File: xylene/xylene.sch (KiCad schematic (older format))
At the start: 19 parts, among them J1 Conn2, J2 Conn1, U1 DIP-8, U2 LMC555, U3 DIP-16

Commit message: Change 555 to SO-8
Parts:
- U2: footprint Package_SO:VSSOP-8_3.0x3.0mm_P0.65mm -> Package_SO:SO-8_3.9x4.9mm_P1.27mm
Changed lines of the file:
@@
 F 0 "U2" H 5550 5600 50  0000 C CNN
 F 1 "LMC555" H 6050 5600 50  0000 C CNN
-F 2 "Package_SO:VSSOP-8_3.0x3.0mm_P0.65mm" H 6700 4850 50  0001 C CNN
+F 2 "Package_SO:SO-8_3.9x4.9mm_P1.27mm" H 6700 4850 50  0001 C CNN
 F 3 "http://www.ti.com/lit/ds/symlink/lmc555.pdf" H 6700 4850 50  0001 C CNN
 	1    5850 5250

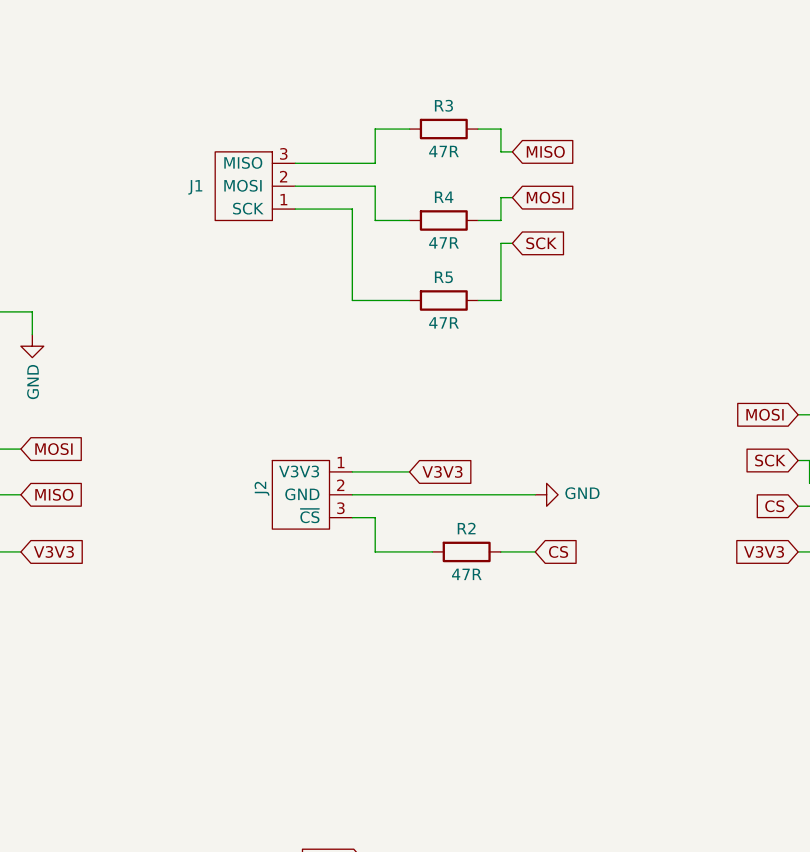
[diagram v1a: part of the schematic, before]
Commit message: Add second pins for logic analyzer
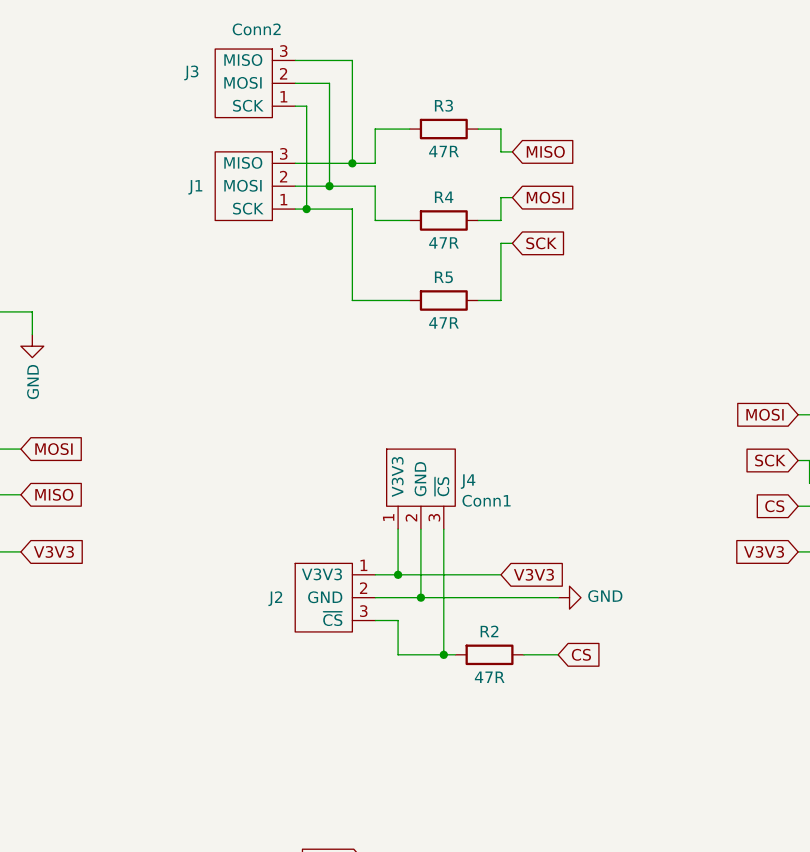
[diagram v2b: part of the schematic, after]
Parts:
- added J3: Conn2, Connector_PinHeader_2.54mm:PinHeader_1x03_P2.54mm_Vertical, symbol xylene:Conn2
- added J4: Conn1, Connector_PinHeader_2.54mm:PinHeader_1x03_P2.54mm_Vertical, symbol xylene:Conn1
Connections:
- net GND: now also J4.2 (GND)
- net V3V3: now also J4.1 (V3V3)
- net at J2.3 (~CS), R2.2: now also J4.3 (~CS)
- net at J1.3 (MISO), R3.2: now also J3.3 (MISO)
- net at J1.2 (MOSI), R4.2: now also J3.2 (MOSI)
- net at J1.1 (SCK), R5.2: now also J3.1 (SCK)
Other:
- moved on the sheet: J2, R2
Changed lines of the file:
@@
 L xylene:Conn1 J2
 U 1 1 5FE8D895
-P 5450 2850
-F 0 "J2" V 5650 2850 50  0000 L CNN
-F 1 "Conn1" V 5462 3038 50  0001 L CNN
-F 2 "Connector_PinHeader_2.54mm:PinHeader_1x03_P2.54mm_Vertical" H 5350 3150 50  0001 C CNN
-F 3 "" H 5350 3150 50  0001 C CNN
-	1    5450 2850
+P 5550 3300
+F 0 "J2" H 5750 3300 50  0000 L CNN
+F 1 "Conn1" V 5562 3488 50  0001 L CNN
+F 2 "Connector_PinHeader_2.54mm:PinHeader_1x03_P2.54mm_Vertical" H 5450 3600 50  0001 C CNN
+F 3 "" H 5450 3600 50  0001 C CNN
+	1    5550 3300
 	-1   0    0    -1
 $EndComp
-Text GLabel 5900 2750 2    50   Input ~ 0
+Text GLabel 6300 3200 2    50   Input ~ 0
 V3V3
 $Comp
 L power:GND #PWR05
 U 1 1 5FF3947C
-P 6450 2850
-F 0 "#PWR05" H 6450 2600 50  0001 C CNN
-F 1 "GND" V 6455 2722 50  0000 R CNN
-F 2 "" H 6450 2850 50  0001 C CNN
-F 3 "" H 6450 2850 50  0001 C CNN
-	1    6450 2850
+P 6550 3300
+F 0 "#PWR05" H 6550 3050 50  0001 C CNN
+F 1 "GND" V 6555 3172 50  0000 R CNN
+F 2 "" H 6550 3300 50  0001 C CNN
+F 3 "" H 6550 3300 50  0001 C CNN
+	1    6550 3300
 	0    -1   -1   0
 $EndComp
@@
 $EndComp
 Wire Wire Line
-	5750 3100 6000 3100
-Wire Wire Line
-	5400 1400 5750 1400
+	5850 3550 6050 3550
+Wire Wire Line
+	5400 1400 5650 1400
 Wire Wire Line
 	5750 1400 5750 1250
@@
 	5750 1650 5750 1500
 Wire Wire Line
-	5750 1500 5400 1500
-Wire Wire Line
-	5400 1600 5650 1600
+	5750 1500 5550 1500
+Wire Wire Line
+	5400 1600 5450 1600
 Wire Wire Line
 	5650 1600 5650 2000
@@
 L Device:R R2
 U 1 1 5FE6703E
-P 6150 3100
-F 0 "R2" V 6050 3100 50  0000 C CNN
-F 1 "47R" V 6250 3100 50  0000 C CNN
-F 2 "Resistor_SMD:R_0603_1608Metric" V 6080 3100 50  0001 C CNN
-F 3 "~" H 6150 3100 50  0001 C CNN
-	1    6150 3100
+P 6250 3550
+F 0 "R2" V 6150 3550 50  0000 C CNN
+F 1 "47R" V 6350 3550 50  0000 C CNN
+F 2 "Resistor_SMD:R_0603_1608Metric" V 6180 3550 50  0001 C CNN
+F 3 "~" H 6250 3550 50  0001 C CNN
+	1    6250 3550
 	0    1    1    0
 $EndComp
@@
 Text GLabel 6350 1350 2    50   Input ~ 0
 MISO
-Text GLabel 6450 3100 2    50   Input ~ 0
+Text GLabel 6550 3550 2    50   Input ~ 0
 CS
 $Comp
@@
 	3950 2050 4250 2050
 Wire Wire Line
-	5650 2750 5900 2750
+	5750 3200 5850 3200
 Wire Wire Line
 	8000 3100 7750 3100
@@
 $EndComp
 Wire Wire Line
-	6300 3100 6450 3100
-Wire Wire Line
-	5650 2950 5750 2950
-Wire Wire Line
-	5750 2950 5750 3100
-Wire Wire Line
-	6450 2850 5650 2850
+	6400 3550 6550 3550
+Wire Wire Line
+	5750 3400 5850 3400
+Wire Wire Line
+	5850 3400 5850 3550
+Wire Wire Line
+	6550 3300 5950 3300
 $Comp
 L xylene:spi_flash_dip_8 U1
@@
 	1    0    0    -1
 $EndComp
+$Comp
+L xylene:Conn1 J4
+U 1 1 60875628
+P 5950 2800
+F 0 "J4" V 5963 2622 50  0000 R CNN
+F 1 "Conn1" V 5872 2622 50  0000 R CNN
+F 2 "Connector_PinHeader_2.54mm:PinHeader_1x03_P2.54mm_Vertical" H 5800 3100 50  0001 C CNN
+F 3 "" H 5800 3100 50  0001 C CNN
+	1    5950 2800
+	0    -1   -1   0
+$EndComp
+Wire Wire Line
+	5850 3000 5850 3200
+Connection ~ 5850 3200
+Wire Wire Line
+	5850 3200 6300 3200
+Wire Wire Line
+	5950 3000 5950 3300
+Connection ~ 5950 3300
+Wire Wire Line
+	5950 3300 5750 3300
+Wire Wire Line
+	6050 3000 6050 3550
+Connection ~ 6050 3550
+Wire Wire Line
+	6050 3550 6100 3550
+$Comp
+L xylene:Conn2 J3
+U 1 1 60889002
+P 5100 1050
+F 0 "J3" H 4950 1100 50  0000 C CNN
+F 1 "Conn2" H 5233 1284 50  0000 C CNN
+F 2 "Connector_PinHeader_2.54mm:PinHeader_1x03_P2.54mm_Vertical" H 5000 1350 50  0001 C CNN
+F 3 "" H 5000 1350 50  0001 C CNN
+	1    5100 1050
+	1    0    0    -1
+$EndComp
+Wire Wire Line
+	5450 1150 5400 1150
+Wire Wire Line
+	5450 1150 5450 1600
+Connection ~ 5450 1600
+Wire Wire Line
+	5450 1600 5650 1600
+Wire Wire Line
+	5550 1500 5550 1050
+Wire Wire Line
+	5550 1050 5400 1050
+Connection ~ 5550 1500
+Wire Wire Line
+	5550 1500 5400 1500
+Wire Wire Line
+	5650 1400 5650 950
+Wire Wire Line
+	5650 950  5400 950
+Connection ~ 5650 1400
+Wire Wire Line
+	5650 1400 5750 1400
 $EndSCHEMATC
